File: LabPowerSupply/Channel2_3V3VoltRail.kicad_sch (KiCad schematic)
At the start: 3 parts

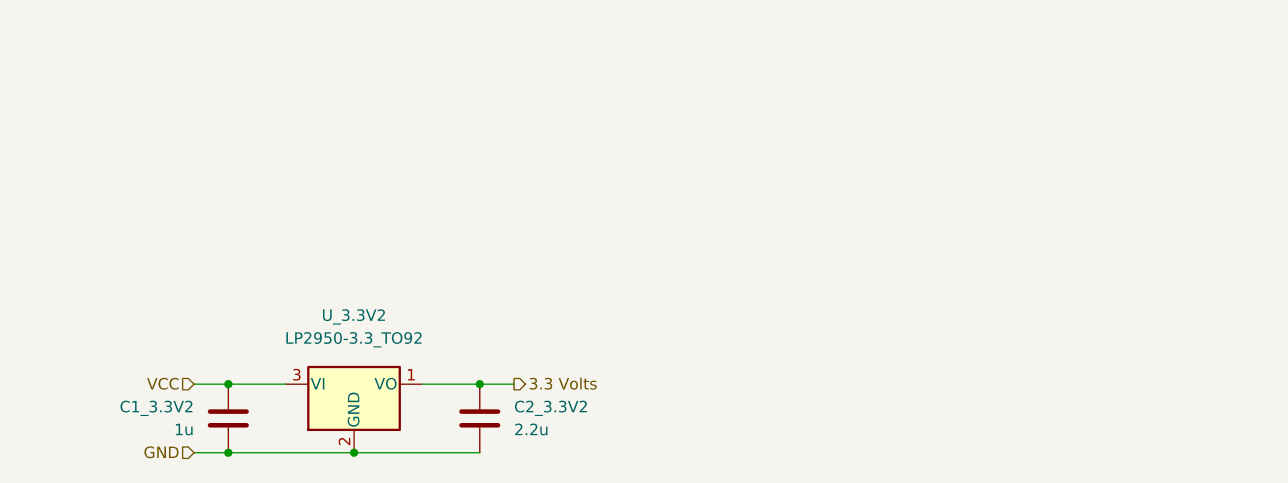
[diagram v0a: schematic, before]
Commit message: Pre regulate 3.3v
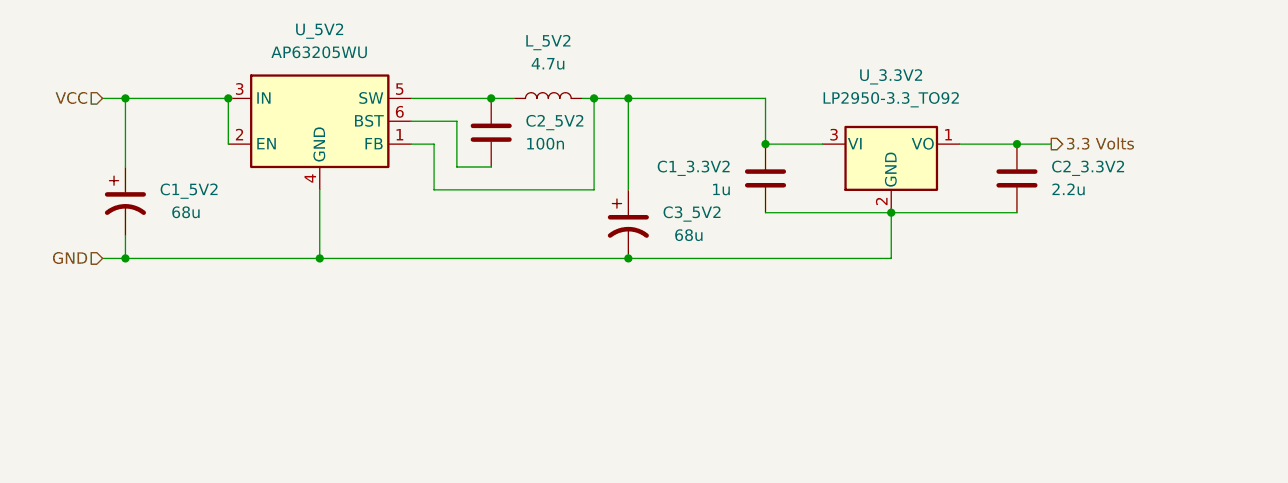
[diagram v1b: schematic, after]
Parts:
- added C1_5V2, C3_5V2: 68u, Capacitor_THT:CP_Radial_D8.0mm_P3.50mm, symbol Device:C_Polarized_US
- added C2_5V2: 100n, Capacitor_SMD:C_0603_1608Metric, symbol Device:C
- added L_5V2: 4.7u, Inductor_SMD:L_Sumida_CDMC6D28_7.25x6.5mm, symbol Device:L
- added U_5V2: AP63205WU, Package_TO_SOT_SMD:TSOT-23-6, symbol Regulator_Switching:AP63205WU
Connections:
- net GND: now also C1_5V2.2, C3_5V2.2, U_5V2.4 (GND)
- net VCC: now also C1_5V2.1, U_5V2.2 (EN), U_5V2.3 (IN); no longer C1_3.3V2.2, U_3.3V2.3 (VI)
- new net: C2_5V2.1, L_5V2.1, U_5V2.5 (SW)
- new net: C2_5V2.2, U_5V2.6 (BST)
- new net: C1_3.3V2.2, C3_5V2.1, L_5V2.2, U_3.3V2.3 (VI), U_5V2.1 (FB)
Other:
- moved on the sheet: C1_3.3V2, C2_3.3V2, U_3.3V2

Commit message: Changed capacitors to x7r
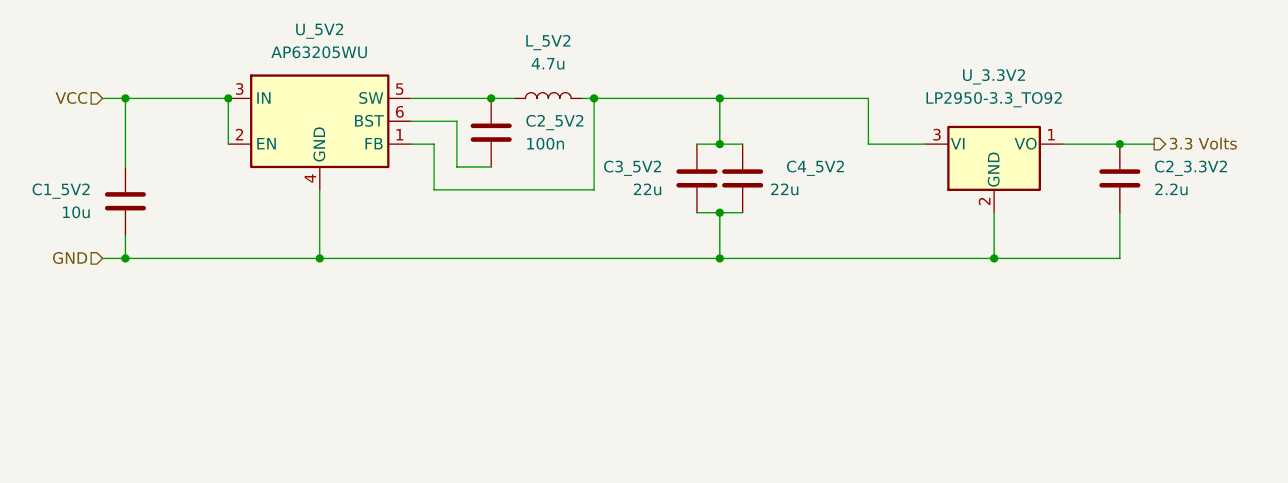
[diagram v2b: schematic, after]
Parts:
- removed C1_3.3V2: 1u, Capacitor_SMD:C_0603_1608Metric, symbol Device:C
- removed C1_5V2, C3_5V2: 68u, Capacitor_THT:CP_Radial_D8.0mm_P3.50mm, symbol Device:C_Polarized_US
- added C1_5V2: 10u, Capacitor_SMD:C_1210_3225Metric, symbol Device:C
- added C3_5V2, C4_5V2: 22u, Capacitor_SMD:C_1210_3225Metric, symbol Device:C
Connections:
- net GND: now also C1_5V2.1, C3_5V2.1, C4_5V2.1
- net VCC: now also C1_5V2.2
- net at L_5V2.2, U_3.3V2.3 (VI), U_5V2.1 (FB): now also C3_5V2.2, C4_5V2.2
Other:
- moved on the sheet: C2_3.3V2, U_3.3V2

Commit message: Fixed cap footprints
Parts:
- C1_5V2: footprint Capacitor_SMD:C_1210_3225Metric -> Capacitor_SMD:C_1206_3216Metric
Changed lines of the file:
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@@
       (effects (font (size 1.27 1.27)) (justify right))
     )
-    (property "Footprint" "Capacitor_SMD:C_1210_3225Metric" (id 2) (at 116.5352 77.47 0)
+    (property "Footprint" "Capacitor_SMD:C_1206_3216Metric" (id 2) (at 116.5352 77.47 0)
       (effects (font (size 1.27 1.27)) hide)
     )

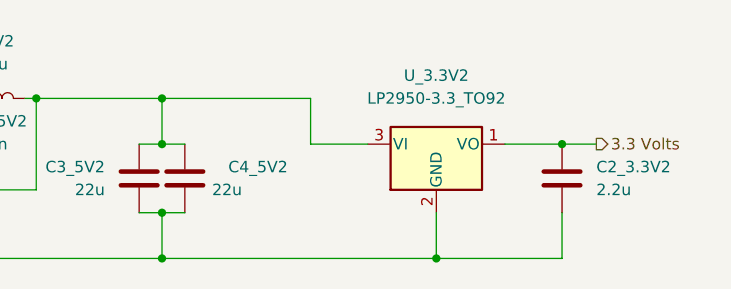
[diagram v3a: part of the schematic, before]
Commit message: Changed grid size, began regrouping
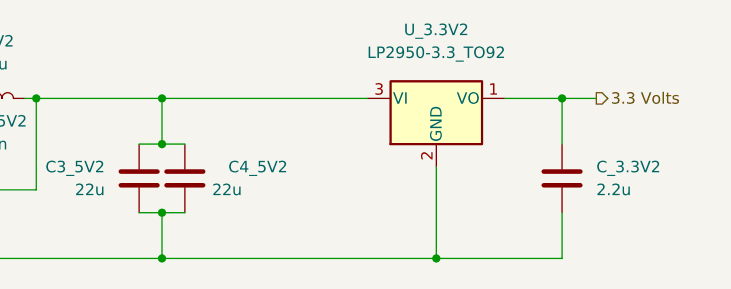
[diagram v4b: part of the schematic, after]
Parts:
- renumbered C2_3.3V2 to C_3.3V2
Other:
- moved on the sheet: U_3.3V2
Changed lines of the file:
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@@
   (junction (at 167.64 69.85) (diameter 0) (color 0 0 0 0)
   )
+  (junction (at 226.06 69.85) (diameter 0) (color 0 0 0 0)
+  )
   (junction (at 137.16 87.63) (diameter 0) (color 0 0 0 0)
   )
   (junction (at 115.57 87.63) (diameter 0) (color 0 0 0 0)
   )
-  (junction (at 226.06 74.93) (diameter 0) (color 0 0 0 0)
-  )
   (junction (at 181.61 87.63) (diameter 0) (color 0 0 0 0)
   )
@@
     (stroke (width 0) (type default) (color 0 0 0 0))
   )
+  (wire (pts (xy 226.06 69.85) (xy 226.06 74.93))
+    (stroke (width 0) (type default) (color 0 0 0 0))
+  )
   (wire (pts (xy 167.64 80.01) (xy 149.86 80.01))
     (stroke (width 0) (type default) (color 0 0 0 0))
   )
-  (wire (pts (xy 212.09 87.63) (xy 212.09 82.55))
-    (stroke (width 0) (type default) (color 0 0 0 0))
-  )
-  (wire (pts (xy 198.12 74.93) (xy 204.47 74.93))
+  (wire (pts (xy 226.06 69.85) (xy 229.87 69.85))
+    (stroke (width 0) (type default) (color 0 0 0 0))
+  )
+  (wire (pts (xy 212.09 87.63) (xy 212.09 77.47))
     (stroke (width 0) (type default) (color 0 0 0 0))
   )
@@
     (stroke (width 0) (type default) (color 0 0 0 0))
   )
-  (wire (pts (xy 219.71 74.93) (xy 226.06 74.93))
-    (stroke (width 0) (type default) (color 0 0 0 0))
-  )
   (wire (pts (xy 113.03 69.85) (xy 115.57 69.85))
     (stroke (width 0) (type default) (color 0 0 0 0))
   )
-  (wire (pts (xy 198.12 69.85) (xy 198.12 74.93))
-    (stroke (width 0) (type default) (color 0 0 0 0))
-  )
   (wire (pts (xy 156.21 77.47) (xy 152.4 77.47))
     (stroke (width 0) (type default) (color 0 0 0 0))
@@
     (stroke (width 0) (type default) (color 0 0 0 0))
   )
-  (wire (pts (xy 226.06 74.93) (xy 229.87 74.93))
-    (stroke (width 0) (type default) (color 0 0 0 0))
-  )
   (wire (pts (xy 166.37 69.85) (xy 167.64 69.85))
     (stroke (width 0) (type default) (color 0 0 0 0))
@@
     (stroke (width 0) (type default) (color 0 0 0 0))
   )
-  (wire (pts (xy 181.61 69.85) (xy 198.12 69.85))
+  (wire (pts (xy 219.71 69.85) (xy 226.06 69.85))
+    (stroke (width 0) (type default) (color 0 0 0 0))
+  )
+  (wire (pts (xy 181.61 69.85) (xy 204.47 69.85))
     (stroke (width 0) (type default) (color 0 0 0 0))
   )
@@
     (effects (font (size 1.27 1.27)) (justify right))
   )
-  (hierarchical_label "3.3 Volts" (shape output) (at 229.87 74.93 0)
+  (hierarchical_label "3.3 Volts" (shape output) (at 229.87 69.85 0)
     (effects (font (size 1.27 1.27)) (justify left))
   )
@@
     (pin "2")
   )
-  (symbol (lib_id "Regulator_Linear:LP2950-3.3_TO92") (at 212.09 74.93 0) (unit 1)
-    (in_bom yes) (on_board yes) (fields_autoplaced)
-    (property "Reference" "U_3.3V2" (id 0) (at 212.09 67.31 0))
-    (property "Value" "LP2950-3.3_TO92" (id 1) (at 212.09 69.85 0))
-    (property "Footprint" "Package_TO_SOT_SMD:TO-252-3_TabPin4" (id 2) (at 212.09 69.215 0)
+  (symbol (lib_id "Regulator_Linear:LP2950-3.3_TO92") (at 212.09 69.85 0) (unit 1)
+    (in_bom yes) (on_board yes) (fields_autoplaced)
+    (property "Reference" "U_3.3V2" (id 0) (at 212.09 62.23 0))
+    (property "Value" "LP2950-3.3_TO92" (id 1) (at 212.09 64.77 0))
+    (property "Footprint" "Package_TO_SOT_SMD:TO-252-3_TabPin4" (id 2) (at 212.09 64.135 0)
       (effects (font (size 1.27 1.27) italic) hide)
     )
-    (property "Datasheet" "http://www.ti.com/lit/ds/symlink/lp2950.pdf" (id 3) (at 212.09 76.2 0)
+    (property "Datasheet" "http://www.ti.com/lit/ds/symlink/lp2950.pdf" (id 3) (at 212.09 71.12 0)
       (effects (font (size 1.27 1.27)) hide)
     )
@@
   (symbol (lib_id "Device:C") (at 226.06 78.74 0) (unit 1)
     (in_bom yes) (on_board yes) (fields_autoplaced)
-    (property "Reference" "C2_3.3V2" (id 0) (at 229.87 77.4699 0)
+    (property "Reference" "C_3.3V2" (id 0) (at 229.87 77.4699 0)
       (effects (font (size 1.27 1.27)) (justify left))
     )

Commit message: routing is weird
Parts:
- renumbered C4_5V2 to C1_3V2, C_3.3V2 to C2_3V2, U_3.3V2 to U_3V2
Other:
- moved on the sheet: C1_3V2
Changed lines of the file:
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@@
   (junction (at 127 69.85) (diameter 0) (color 0 0 0 0)
   )
+  (junction (at 195.58 69.85) (diameter 0) (color 0 0 0 0)
+  )
   (junction (at 212.09 87.63) (diameter 0) (color 0 0 0 0)
   )
   (junction (at 115.57 69.85) (diameter 0) (color 0 0 0 0)
   )
-  (junction (at 181.61 82.55) (diameter 0) (color 0 0 0 0)
-  )
   (junction (at 167.64 69.85) (diameter 0) (color 0 0 0 0)
   )
+  (junction (at 195.58 87.63) (diameter 0) (color 0 0 0 0)
+  )
   (junction (at 226.06 69.85) (diameter 0) (color 0 0 0 0)
   )
   (junction (at 137.16 87.63) (diameter 0) (color 0 0 0 0)
   )
+  (junction (at 179.07 69.85) (diameter 0) (color 0 0 0 0)
+  )
   (junction (at 115.57 87.63) (diameter 0) (color 0 0 0 0)
   )
-  (junction (at 181.61 87.63) (diameter 0) (color 0 0 0 0)
-  )
-  (junction (at 181.61 69.85) (diameter 0) (color 0 0 0 0)
+  (junction (at 179.07 87.63) (diameter 0) (color 0 0 0 0)
   )
   (junction (at 156.21 69.85) (diameter 0) (color 0 0 0 0)
   )
-  (junction (at 181.61 74.93) (diameter 0) (color 0 0 0 0)
-  )
   (wire (pts (xy 167.64 69.85) (xy 167.64 80.01))
     (stroke (width 0) (type default) (color 0 0 0 0))
@@
     (stroke (width 0) (type default) (color 0 0 0 0))
   )
+  (wire (pts (xy 195.58 69.85) (xy 195.58 74.93))
+    (stroke (width 0) (type default) (color 0 0 0 0))
+  )
   (wire (pts (xy 226.06 82.55) (xy 226.06 87.63))
     (stroke (width 0) (type default) (color 0 0 0 0))
@@
     (stroke (width 0) (type default) (color 0 0 0 0))
   )
-  (wire (pts (xy 181.61 82.55) (xy 184.15 82.55))
-    (stroke (width 0) (type default) (color 0 0 0 0))
-  )
-  (wire (pts (xy 179.07 82.55) (xy 181.61 82.55))
+  (wire (pts (xy 195.58 69.85) (xy 204.47 69.85))
     (stroke (width 0) (type default) (color 0 0 0 0))
   )
@@
     (stroke (width 0) (type default) (color 0 0 0 0))
   )
+  (wire (pts (xy 195.58 87.63) (xy 212.09 87.63))
+    (stroke (width 0) (type default) (color 0 0 0 0))
+  )
   (wire (pts (xy 156.21 77.47) (xy 152.4 77.47))
     (stroke (width 0) (type default) (color 0 0 0 0))
   )
-  (wire (pts (xy 181.61 69.85) (xy 181.61 74.93))
-    (stroke (width 0) (type default) (color 0 0 0 0))
-  )
-  (wire (pts (xy 181.61 74.93) (xy 184.15 74.93))
-    (stroke (width 0) (type default) (color 0 0 0 0))
-  )
-  (wire (pts (xy 181.61 82.55) (xy 181.61 87.63))
+  (wire (pts (xy 179.07 69.85) (xy 179.07 74.93))
     (stroke (width 0) (type default) (color 0 0 0 0))
   )
@@
     (stroke (width 0) (type default) (color 0 0 0 0))
   )
+  (wire (pts (xy 179.07 69.85) (xy 195.58 69.85))
+    (stroke (width 0) (type default) (color 0 0 0 0))
+  )
   (wire (pts (xy 166.37 69.85) (xy 167.64 69.85))
     (stroke (width 0) (type default) (color 0 0 0 0))
   )
-  (wire (pts (xy 179.07 74.93) (xy 181.61 74.93))
-    (stroke (width 0) (type default) (color 0 0 0 0))
-  )
-  (wire (pts (xy 167.64 69.85) (xy 181.61 69.85))
+  (wire (pts (xy 167.64 69.85) (xy 179.07 69.85))
+    (stroke (width 0) (type default) (color 0 0 0 0))
+  )
+  (wire (pts (xy 179.07 82.55) (xy 179.07 87.63))
+    (stroke (width 0) (type default) (color 0 0 0 0))
+  )
+  (wire (pts (xy 195.58 82.55) (xy 195.58 87.63))
+    (stroke (width 0) (type default) (color 0 0 0 0))
+  )
+  (wire (pts (xy 179.07 87.63) (xy 195.58 87.63))
     (stroke (width 0) (type default) (color 0 0 0 0))
   )
@@
     (stroke (width 0) (type default) (color 0 0 0 0))
   )
-  (wire (pts (xy 181.61 69.85) (xy 204.47 69.85))
-    (stroke (width 0) (type default) (color 0 0 0 0))
-  )
   (wire (pts (xy 113.03 87.63) (xy 115.57 87.63))
     (stroke (width 0) (type default) (color 0 0 0 0))
   )
-  (wire (pts (xy 137.16 87.63) (xy 181.61 87.63))
-    (stroke (width 0) (type default) (color 0 0 0 0))
-  )
-  (wire (pts (xy 181.61 87.63) (xy 212.09 87.63))
+  (wire (pts (xy 137.16 87.63) (xy 179.07 87.63))
     (stroke (width 0) (type default) (color 0 0 0 0))
   )
@@
     (pin "6")
   )
-  (symbol (lib_id "Device:C") (at 184.15 78.74 0) (mirror x) (unit 1)
+  (symbol (lib_id "Device:C") (at 195.58 78.74 0) (mirror x) (unit 1)
     (in_bom yes) (on_board yes)
-    (property "Reference" "C4_5V2" (id 0) (at 195.58 77.47 0)
-      (effects (font (size 1.27 1.27)) (justify right))
-    )
-    (property "Value" "22u" (id 1) (at 190.5 80.01 0)
-      (effects (font (size 1.27 1.27)) (justify right))
-    )
-    (property "Footprint" "Capacitor_SMD:C_1210_3225Metric" (id 2) (at 185.1152 74.93 0)
-      (effects (font (size 1.27 1.27)) hide)
-    )
-    (property "Datasheet" "~" (id 3) (at 184.15 78.74 0)
+    (property "Reference" "C1_3V2" (id 0) (at 207.01 77.47 0)
+      (effects (font (size 1.27 1.27)) (justify right))
+    )
+    (property "Value" "22u" (id 1) (at 201.93 80.01 0)
+      (effects (font (size 1.27 1.27)) (justify right))
+    )
+    (property "Footprint" "Capacitor_SMD:C_1210_3225Metric" (id 2) (at 196.5452 74.93 0)
+      (effects (font (size 1.27 1.27)) hide)
+    )
+    (property "Datasheet" "~" (id 3) (at 195.58 78.74 0)
       (effects (font (size 1.27 1.27)) hide)
     )
@@
   (symbol (lib_id "Regulator_Linear:LP2950-3.3_TO92") (at 212.09 69.85 0) (unit 1)
     (in_bom yes) (on_board yes) (fields_autoplaced)
-    (property "Reference" "U_3.3V2" (id 0) (at 212.09 62.23 0))
+    (property "Reference" "U_3V2" (id 0) (at 212.09 62.23 0))
     (property "Value" "LP2950-3.3_TO92" (id 1) (at 212.09 64.77 0))
     (property "Footprint" "Package_TO_SOT_SMD:TO-252-3_TabPin4" (id 2) (at 212.09 64.135 0)
@@
   (symbol (lib_id "Device:C") (at 226.06 78.74 0) (unit 1)
     (in_bom yes) (on_board yes) (fields_autoplaced)
-    (property "Reference" "C_3.3V2" (id 0) (at 229.87 77.4699 0)
+    (property "Reference" "C2_3V2" (id 0) (at 229.87 77.4699 0)
       (effects (font (size 1.27 1.27)) (justify left))
     )

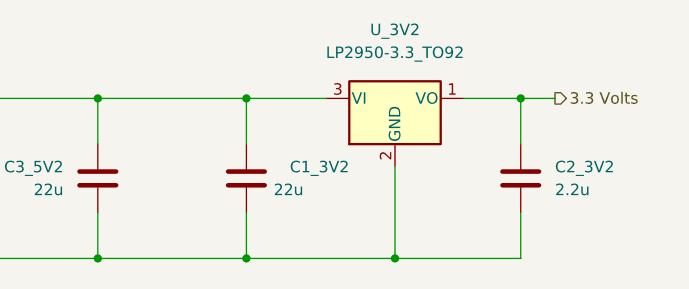
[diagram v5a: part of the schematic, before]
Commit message: Fixed 3.3v footprint
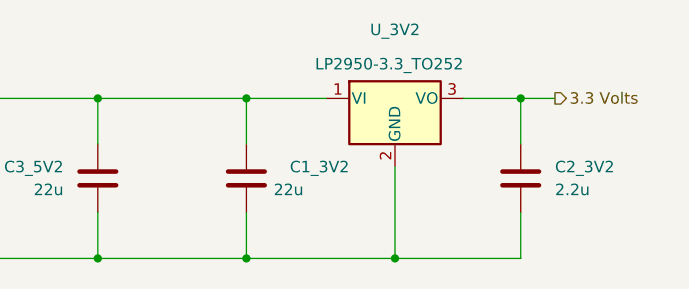
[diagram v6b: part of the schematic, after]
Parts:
- U_3V2: value LP2950-3.3_TO92 -> LP2950-3.3_TO252; footprint Package_TO_SOT_SMD:TO-252-3_TabPin4 -> Package_TO_SOT_SMD:TO-252-2; symbol Regulator_Linear:LP2950-3.3_TO92 -> Regulator_Linear:LP2950-3.3_TO252
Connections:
- net 3.3 Volts: now also U_3V2.3 (VO); no longer U_3V2.1 (VO)
- net at C1_3V2.2, C3_5V2.2, L_5V2.2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: now also U_3V2.1 (VI); no longer U_3V2.3 (VI)
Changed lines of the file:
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@@
     (pin "2")
   )
-  (symbol (lib_id "Regulator_Linear:LP2950-3.3_TO92") (at 212.09 69.85 0) (unit 1)
-    (in_bom yes) (on_board yes) (fields_autoplaced)
+  (symbol (lib_id "Regulator_Linear:LP2950-3.3_TO252") (at 212.09 69.85 0) (unit 1)
+    (in_bom yes) (on_board yes)
     (property "Reference" "U_3V2" (id 0) (at 212.09 62.23 0))
-    (property "Value" "LP2950-3.3_TO92" (id 1) (at 212.09 64.77 0))
-    (property "Footprint" "Package_TO_SOT_SMD:TO-252-3_TabPin4" (id 2) (at 212.09 64.135 0)
+    (property "Value" "LP2950-3.3_TO252" (id 1) (at 203.2 66.04 0)
+      (effects (font (size 1.27 1.27)) (justify left))
+    )
+    (property "Footprint" "Package_TO_SOT_SMD:TO-252-2" (id 2) (at 212.09 64.135 0)
       (effects (font (size 1.27 1.27) italic) hide)
     )
